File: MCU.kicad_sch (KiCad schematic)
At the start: 14 parts, among them J3 Conn_02x03_Odd_Even, U1 HDC2080, U3 ESP32-C6-MINI-1

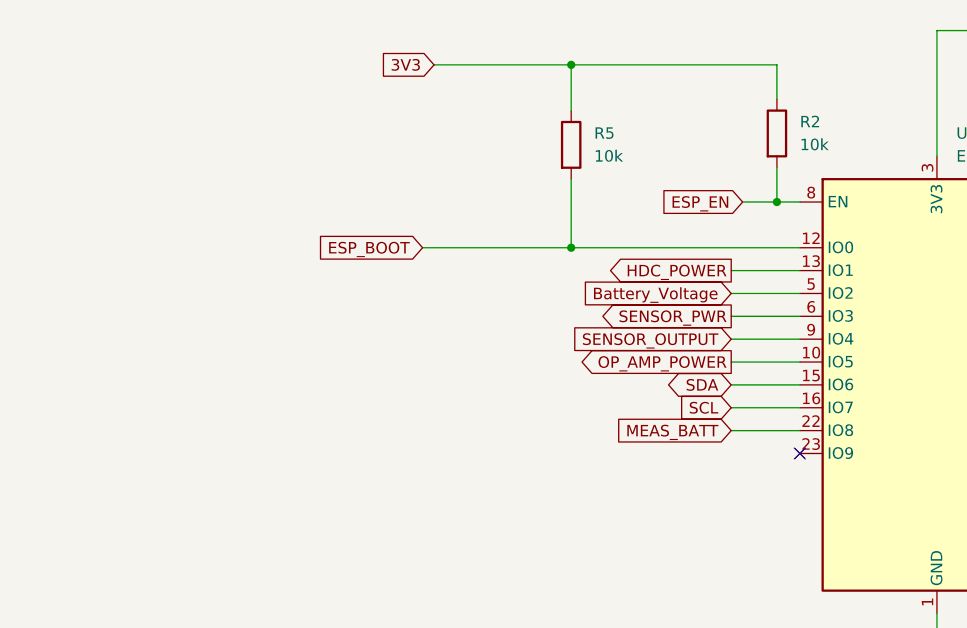
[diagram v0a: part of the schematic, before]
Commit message: Added boot pin strapping
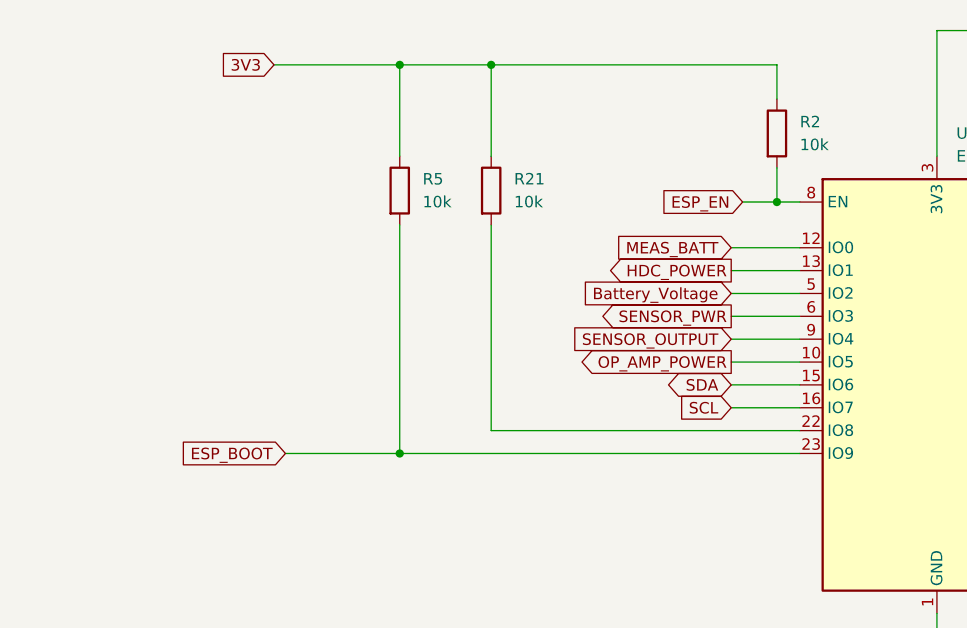
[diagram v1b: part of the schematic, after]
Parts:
- added R21: 10k, Resistor_SMD:R_0805_2012Metric_Pad1.20x1.40mm_HandSolder, symbol Device:R
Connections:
- net 3V3: now also R21.1
- net ESP_BOOT: now also U3.23 (IO9); no longer U3.12 (IO0)
- net MEAS_BATT: now also U3.12 (IO0); no longer U3.22 (IO8)
- new net: R21.2, U3.22 (IO8)
- no-connect marks 7 -> 6
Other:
- moved on the sheet: R5

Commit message: finished board layout for AD revision
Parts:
- removed U3: ESP32-C6-MINI-1, RF_Module:ESP32-C6-MINI-1, symbol RF_Module:ESP32-C6-MINI-1
- added U4: ESP32-C6-WROOM-1-N4, Hydro_footprints:MOD28_ESP32-C6-WROOM-1_EXP, symbol Hydro_symbols:ESP32-C6-WROOM-1-N4
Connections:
- net 3V3: now also U4.2 (3V3)
- net Battery_Voltage: now also U4.27 (IO2)
- net CHARGE_STATUS: now also U4.23 (IO15)
- net ESP_BOOT: now also U4.15 (IO9)
- net ESP_EN: now also U4.3 (EN)
- net GND: now also U4.1 (GND), U4.28 (GND), U4.29 (GND), U4.30 (GND), U4.31 (GND), U4.32 (GND), U4.33 (GND), U4.34 (GND), U4.35 (GND), U4.36 (GND), U4.37 (GND)
- net HDC_INT: now also U4.14 (IO13)
- net HDC_POWER: now also U4.9 (IO1)
- net MEAS_BATT: now also U4.8 (IO0)
- net OP_AMP_POWER: now also U4.5 (IO5)
- net QI_EN2: now also U4.13 (IO12)
- net RXD0: now also U4.24 (RXD0)
- net SCL: now also U4.7 (IO7)
- net SDA: now also U4.6 (IO6)
- net SENSOR_OUTPUT: now also U4.4 (IO4)
- net SENSOR_PWR: now also U4.26 (IO3)
- net TXD0: now also U4.25 (TXD0)
- net at R12.1: now also U4.16 (IO18)
- net at R21.2: now also U4.10 (IO8)
- no-connect marks 6 -> 7
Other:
- moved on the sheet: C1, C2, D3, R12, R2
